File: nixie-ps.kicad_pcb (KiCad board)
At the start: 2 copper layers, 46 x 23 mm, 19 parts, among them J1 Conn_01x04_Male, J2 Conn_01x04_Male, Q1 IRFH5106PBF, T1 EFD15_2WI, U1 LM3488MM

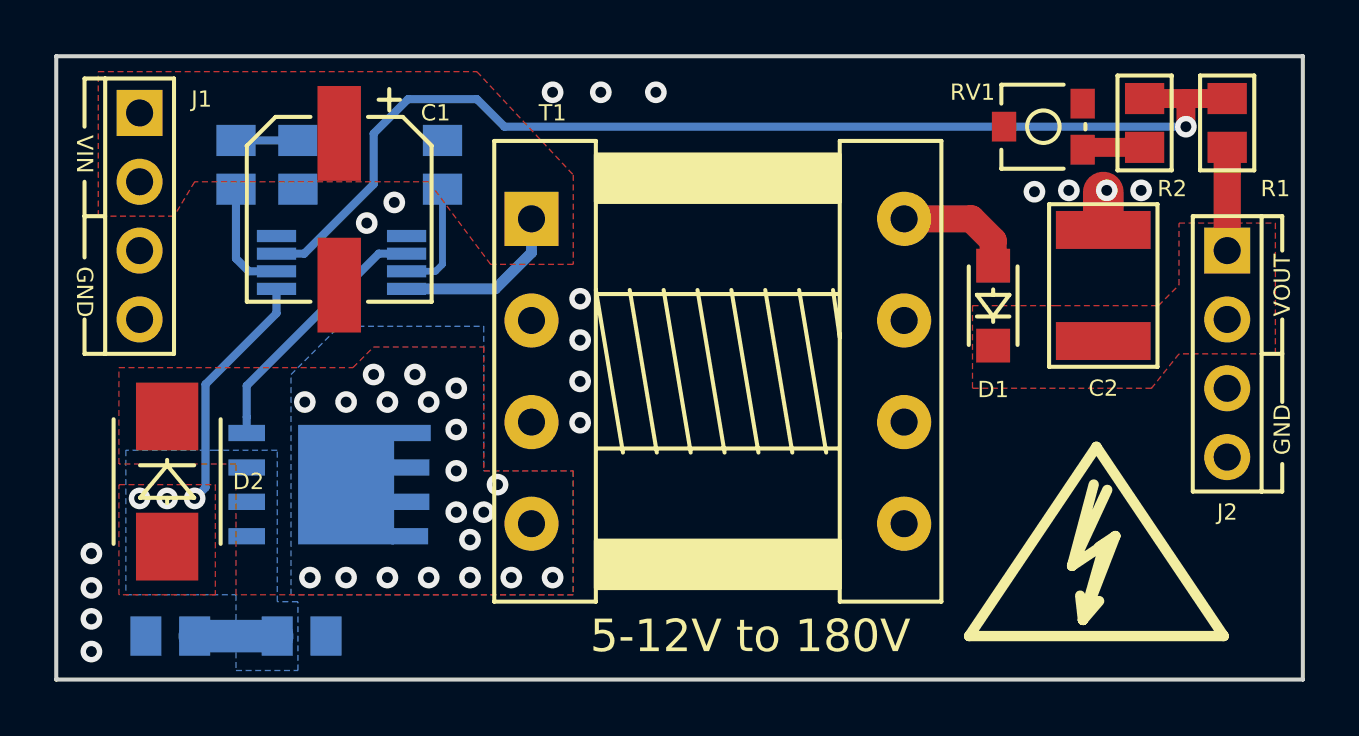
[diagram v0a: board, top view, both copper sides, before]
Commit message: Replace IRFH5106PBF to RFH7185TRPBF Replace resistor Isense footprint to bigger one Also update ltspice scheme with last changes
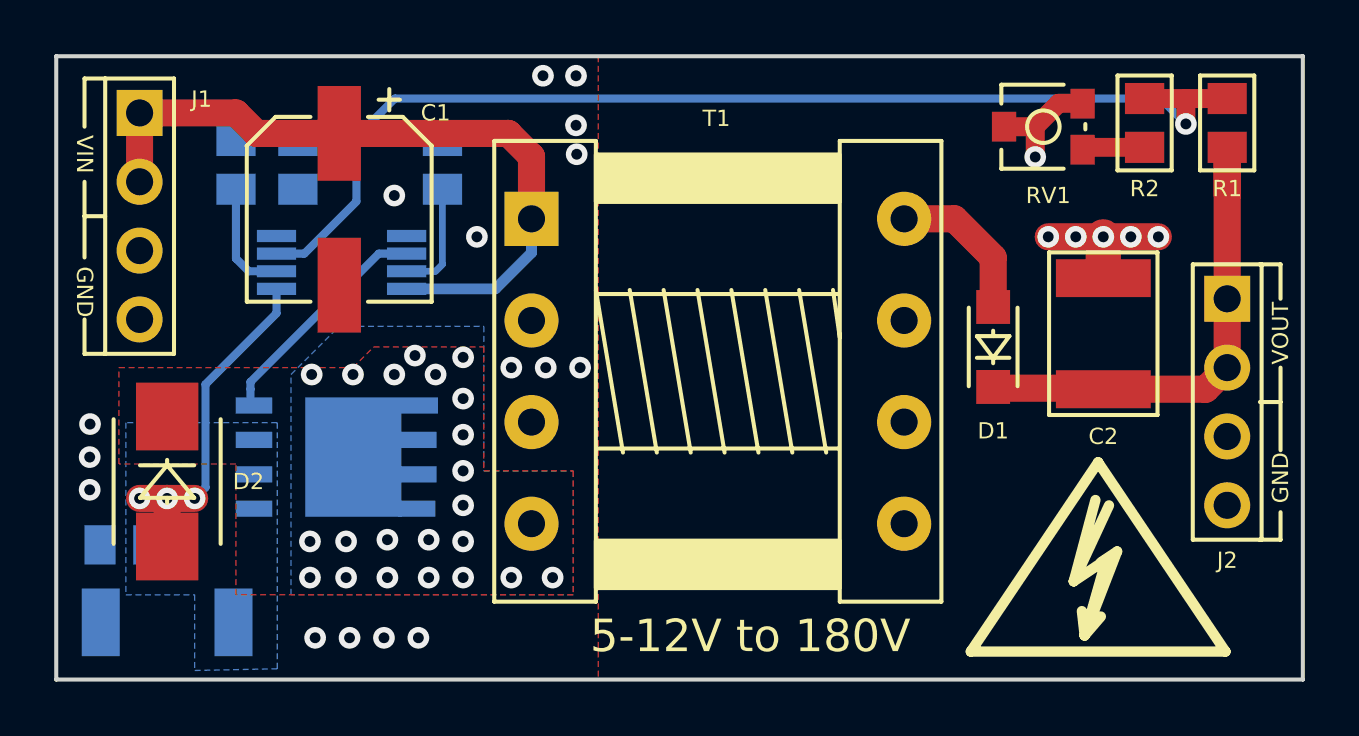
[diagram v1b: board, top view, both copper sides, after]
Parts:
- Q1: value IRFH5106PBF -> IRFH7185TRPBF
- R5: value 0.01 -> 0; footprint lib_fp:0805 -> lib_fp:2010
- moved C4 7.36 mm to (99.5, 117.0), turned to 180 degrees
- moved C2 1.78 mm to (135.6, 109.2)
- moved J2 1.78 mm to (140.2, 108.0)
- moved G*** 1.59 mm to (121.8, 110.2)
- moved D1 1.52 mm to (131.6, 109.7)
- moved Q1 1.05 mm to (107.3, 113.8)
- moved REF** 0.58 mm to (135.4, 118.2)
- moved R5 0.52 mm to (101.1, 119.9)
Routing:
- net /VIN: track 6.41 -> 26.4 mm
- net /VOUT: track 3.81 -> 18.9 mm
- net GND: track 1.45 -> 9.97 mm, vias 17 -> 22
- net Net-(D1-Pad2): track 4.54 -> 5.70 mm
- net /DR: track 9.66 -> 8.59 mm
- net /ISEN: track 12.0 -> 12.8 mm
- net Net-(D2-Pad1): vias 20 -> 22
- removed copper zone on F.Cu, net /ISEN
- removed copper zone on F.Cu, net /VIN
- removed copper zone on F.Cu, net /VOUT
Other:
- net class Power added: clearance 0.2, trace_width 0.7, via_dia 0.8, via_drill 0.4

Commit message: Reroute board left side
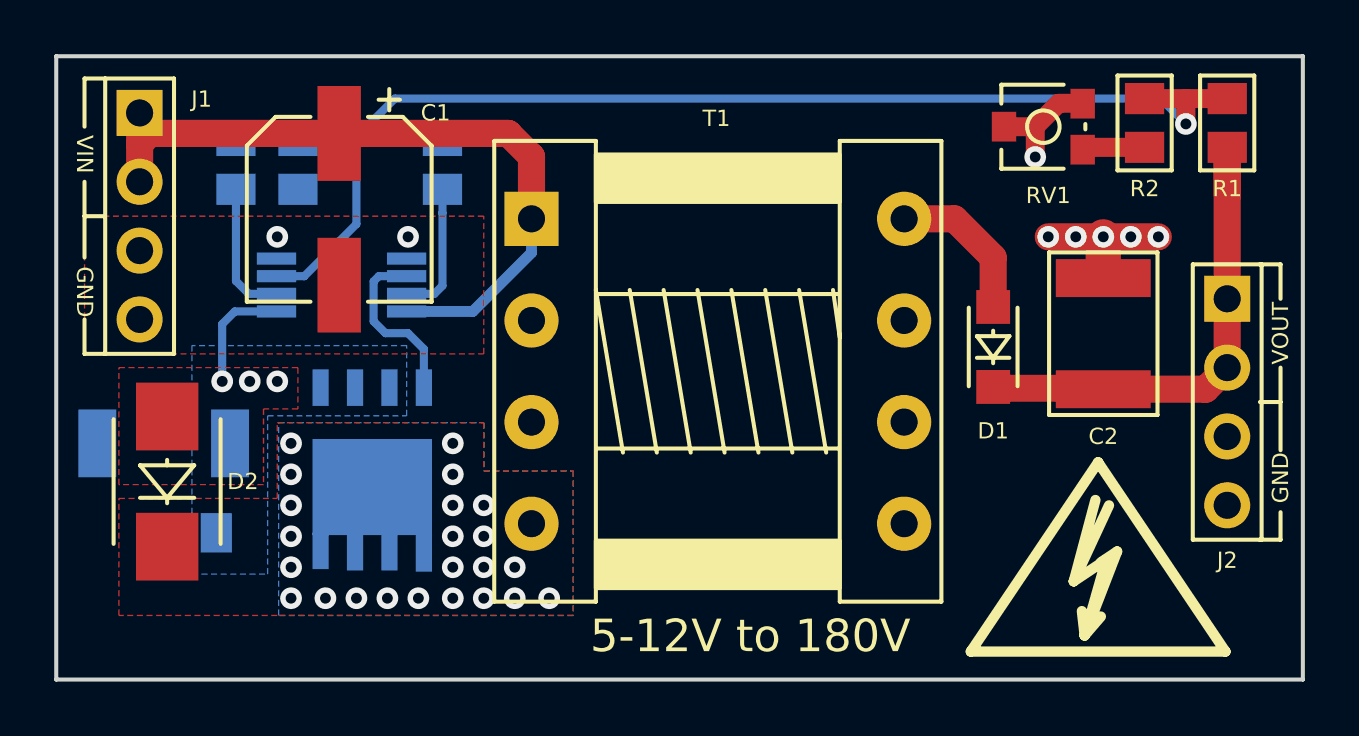
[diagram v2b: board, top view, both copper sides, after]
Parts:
- moved R5 6.61 mm to (101.0, 113.3)
- moved C4 2.53 mm to (102.0, 116.6)
- moved Q1 1.42 mm to (108.7, 114.2), turned to 0 degrees
- moved U1 0.83 mm to (107.5, 107.4)
- turned D2 to 90 degrees
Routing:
- net /ISEN: track 12.8 -> 4.31 mm
- net /VIN: track 26.4 -> 29.6 mm
- net /DR: track 8.59 -> 6.47 mm
- net /FB: track 41.7 -> 42.5 mm
- net /FA: track 4.34 -> 5.01 mm
- net /COMP: track 4.50 -> 5.08 mm
- net Net-(D2-Pad1): vias 22 -> 23
- net GND: vias 22 -> 8
- added copper zone on F.Cu, net /ISEN
